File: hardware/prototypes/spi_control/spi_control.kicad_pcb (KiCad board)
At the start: 2 copper layers, 78 parts, among them J1 USB_B_Micro, J39 Versa_1, J40 Versa_2, U1 ST1L08SPU33R, U2 MCP2210-I_MQ, U3 ADAR7251, U4 BGT24_Module, Y1 12MHZ, Y2 40MHz

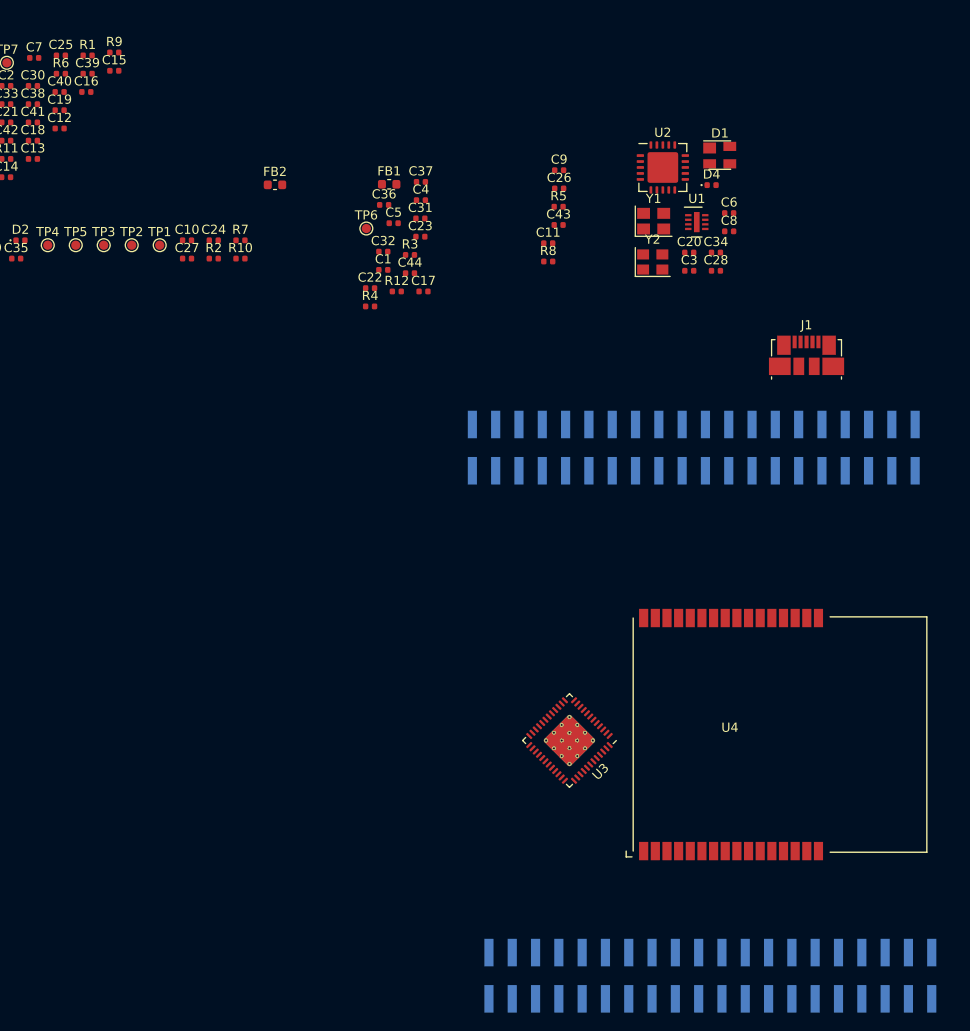
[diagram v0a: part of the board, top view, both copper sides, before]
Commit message: Fixed 3D Model path for the RF castelation board. Added mounting holes for antenna secure.
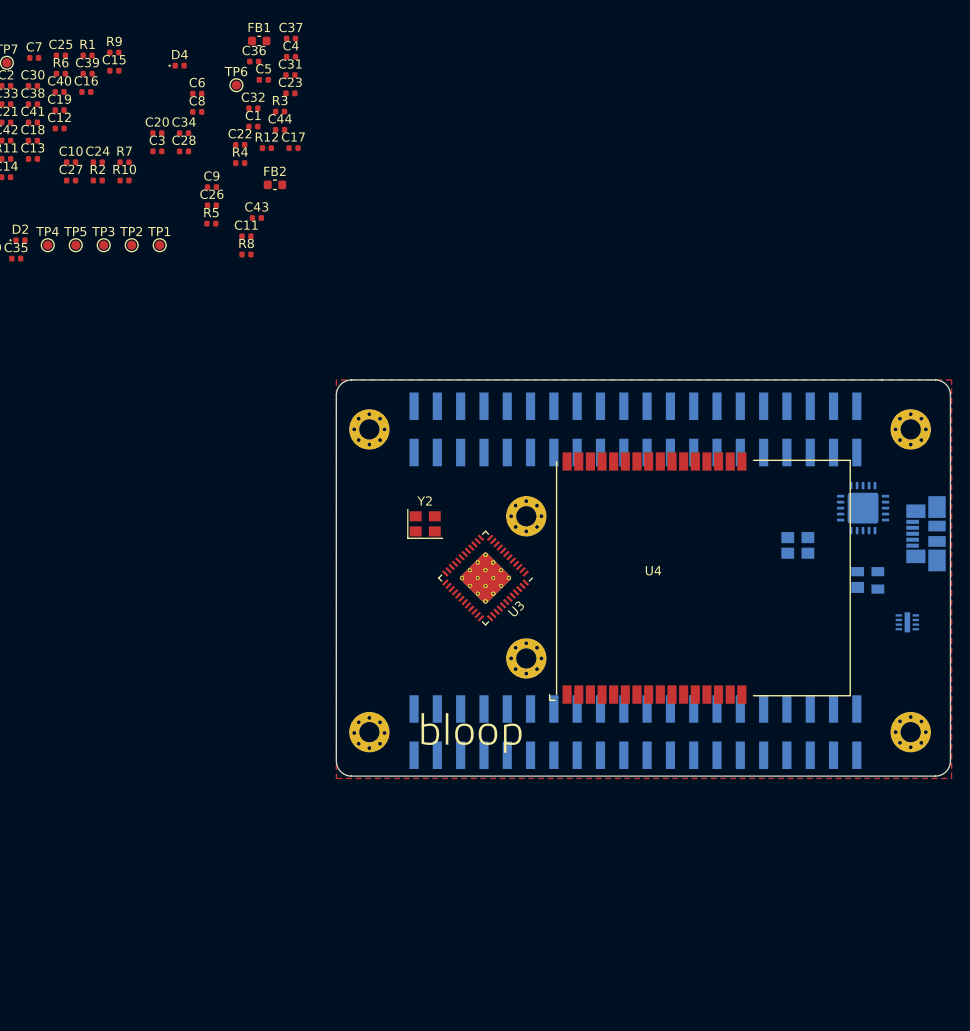
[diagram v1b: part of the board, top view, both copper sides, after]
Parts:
- added REF**: MountingHole_2.2mm_M2_Pad_Via, MountingHole:MountingHole_2.2mm_M2_Pad_Via, F.Cu at (78.1, 85.0)
- added REF**: MountingHole_2.2mm_M2_Pad_Via, MountingHole:MountingHole_2.2mm_M2_Pad_Via, F.Cu at (78.1, 69.5)
- added REF**: MountingHole_2.2mm_M2_Pad_Via, MountingHole:MountingHole_2.2mm_M2_Pad_Via, F.Cu at (120.0, 93.0)
- added REF**: MountingHole_2.2mm_M2_Pad_Via, MountingHole:MountingHole_2.2mm_M2_Pad_Via, F.Cu at (120.0, 60.0)
- added REF**: MountingHole_2.2mm_M2_Pad_Via, MountingHole:MountingHole_2.2mm_M2_Pad_Via, F.Cu at (61.0, 93.1)
- added REF**: MountingHole_2.2mm_M2_Pad_Via, MountingHole:MountingHole_2.2mm_M2_Pad_Via, F.Cu at (61.0, 60.0)
- added ~: LOGO, bloop:bloop_logo_text_silkandcopper, F.Cu at (72.1, 93.2)
- D1, J1, U1, U2, Y1: moved to B.Cu
- moved C20 59.4 mm to (37.9, 27.7)
- moved C28 59.4 mm to (40.8, 29.7)
- moved C3 59.4 mm to (37.9, 29.7)
- moved C34 59.4 mm to (40.8, 27.7)
- moved D4 59.4 mm to (40.3, 20.4)
- moved C6 59.4 mm to (42.2, 23.4)
- moved C8 59.4 mm to (42.2, 25.4)
- moved U1 49.3 mm to (119.6, 81.0)
- moved D1 49.1 mm to (115.3, 76.5)
- moved U2 43.1 mm to (114.8, 68.6)
- moved Y1 38.7 mm to (107.7, 72.6)
- moved C26 37.9 mm to (43.8, 35.6)
- moved C9 37.9 mm to (43.8, 33.6)
- moved R5 37.9 mm to (43.8, 37.6)
- moved Y2 37.8 mm to (67.1, 70.3)
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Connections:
- J39 pad 10: /SCK -> /ADC_DOUT4
- J39 pad 11: Net-(J39-Pad11) -> /MISO
- J39 pad 12: Net-(J39-Pad12) -> /ADC_DOUT3
- J39 pad 13: Net-(J39-Pad13) -> /PLL_DIV_MCU
- J39 pad 14: Net-(J39-Pad14) -> /ADC_DOUT2
- J39 pad 15: Net-(J39-Pad15) -> /PLL_LE
- J39 pad 16: /PLL_CS -> /ADC_DOUT1
- J39 pad 17: Net-(J39-Pad17) -> /PLL_CS
- J39 pad 18: /PLL_LE -> /ADC_DOUT0
- J39 pad 20: /PLL_DIV_MCU -> Net-(J39-Pad20)
- J39 pad 29: Net-(J39-Pad29) -> /~CONV_START
- J39 pad 31: Net-(J39-Pad31) -> /~FAULT
- J39 pad 33: Net-(J39-Pad33) -> /~RESET\PWDN
- J39 pad 4: Net-(J39-Pad4) -> /ADC_DOUT7
- J39 pad 5: Net-(J39-Pad5) -> /SCLK_ADC
- J39 pad 6: /MISO -> /ADC_DOUT6
- J39 pad 7: Net-(J39-Pad7) -> /SCK
- J39 pad 8: /MOSI -> /ADC_DOUT5
- J39 pad 9: Net-(J39-Pad9) -> /MOSI
- J40 pad 1: /ADC_DOUT7 -> /DATA_READY
- J40 pad 11: /ADC_DOUT2 -> Net-(J40-Pad11)
- J40 pad 13: /ADC_DOUT1 -> Net-(J40-Pad13)
- J40 pad 15: /ADC_DOUT0 -> Net-(J40-Pad15)
- J40 pad 17: /SCLK_ADC -> Net-(J40-Pad17)
- J40 pad 3: /ADC_DOUT6 -> Net-(J40-Pad3)
- J40 pad 5: /ADC_DOUT5 -> /MCLKIN
- J40 pad 7: /ADC_DOUT4 -> Net-(J40-Pad7)
- J40 pad 9: /ADC_DOUT3 -> Net-(J40-Pad9)
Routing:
- added copper zone on F.Cu, net GND
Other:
- board outline added: 66.9 x 43.2 mm

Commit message: Aligned all holes to by symmetric and locked their position
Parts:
- moved C11 38.1 mm to (46.3, 77.0)
- moved C20 38.1 mm to (36.6, 65.8)
- moved C21 38.1 mm to (20.2, 64.6)
- moved C22 38.1 mm to (45.6, 67.1)
- moved C33 38.1 mm to (20.2, 62.7)
- moved C34 38.1 mm to (39.5, 65.8)
- moved C38 38.1 mm to (23.1, 62.7)
- moved C41 38.1 mm to (23.1, 64.6)
- moved TP6 38.1 mm to (45.2, 60.6)
- moved C12 38.1 mm to (26.0, 65.3)
- moved C14 38.1 mm to (20.1, 70.6)
- moved C15 38.1 mm to (31.9, 59.0)
- moved C17 38.1 mm to (51.5, 67.4)
- moved C18 38.1 mm to (23.1, 66.6)
- moved C19 38.1 mm to (26.0, 63.3)
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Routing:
- added copper zone on B.Cu, net (none)
- added copper zone on In2.Cu, net +3V3
- added copper zone on In1.Cu, net GND
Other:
- copper layers 2 -> 4
- board text added: "Top - SIGNAL Inner Layer 1 - GND Inner Layer 2 - Power Bottom - SIGNAL"

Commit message: Found error in layer stackup, fixed net for top copper.
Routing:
- added copper zone on F.Cu, net (none)
- removed copper zone on F.Cu, net GND
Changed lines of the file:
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@@
       (xy 1.499932 -3.114028) (xy 1.609258 -3.12054) (xy 1.718859 -3.123741) (xy 1.828668 -3.123619)) (layer F.Mask) (width 0.127))
   )
-  (module MountingHole:MountingHole_2.2mm_M2_Pad_Via (layer F.Cu)
+  (module MountingHole:MountingHole_2.2mm_M2_Pad_Via locked (layer F.Cu)
     (at 77.47 84.411)
     (descr "Mounting Hole 2.2mm, M2")
@@
     (pad 1 thru_hole circle (at 0 0) (size 4.4 4.4) (drill 2.2) (layers *.Cu *.Mask))
   )
-  (module MountingHole:MountingHole_2.2mm_M2_Pad_Via (layer F.Cu)
+  (module MountingHole:MountingHole_2.2mm_M2_Pad_Via locked (layer F.Cu)
     (at 77.47 68.58)
     (descr "Mounting Hole 2.2mm, M2")
@@
     (pad 1 thru_hole circle (at 0 0) (size 4.4 4.4) (drill 2.2) (layers *.Cu *.Mask))
   )
-  (module MountingHole:MountingHole_2.2mm_M2_Pad_Via (layer F.Cu)
+  (module MountingHole:MountingHole_2.2mm_M2_Pad_Via locked (layer F.Cu)
     (at 120 92.9946)
     (descr "Mounting Hole 2.2mm, M2")
@@
     (pad 1 thru_hole circle (at 0 0) (size 4.4 4.4) (drill 2.2) (layers *.Cu *.Mask))
   )
-  (module MountingHole:MountingHole_2.2mm_M2_Pad_Via (layer F.Cu)
+  (module MountingHole:MountingHole_2.2mm_M2_Pad_Via locked (layer F.Cu)
     (at 120 60)
     (descr "Mounting Hole 2.2mm, M2")
@@
     (pad 1 thru_hole circle (at 0 0) (size 4.4 4.4) (drill 2.2) (layers *.Cu *.Mask))
   )
-  (module MountingHole:MountingHole_2.2mm_M2_Pad_Via (layer F.Cu)
+  (module MountingHole:MountingHole_2.2mm_M2_Pad_Via locked (layer F.Cu)
     (at 61 93.091)
     (descr "Mounting Hole 2.2mm, M2")
@@
     (pad 1 thru_hole circle (at 0 -0.0964) (size 4.4 4.4) (drill 2.2) (layers *.Cu *.Mask))
   )
-  (module MountingHole:MountingHole_2.2mm_M2_Pad_Via (layer F.Cu)
+  (module MountingHole:MountingHole_2.2mm_M2_Pad_Via locked (layer F.Cu)
     (at 61 60)
     (descr "Mounting Hole 2.2mm, M2")
@@
     )
   )
-  (zone (net 1) (net_name GND) (layer F.Cu) (hatch edge 0.508)
+  (zone (net 0) (net_name "") (layer F.Cu) (hatch edge 0.508)
     (connect_pads yes (clearance 0.3))
     (min_thickness 0.254)

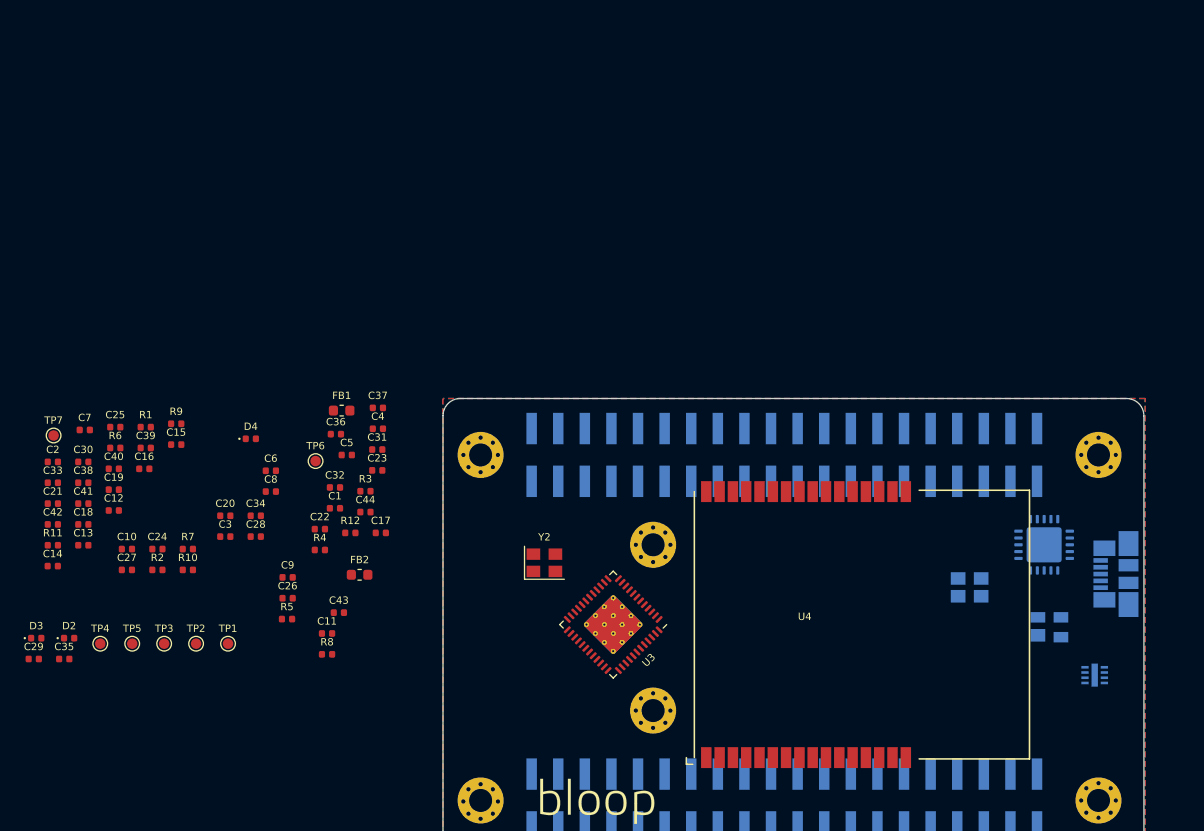
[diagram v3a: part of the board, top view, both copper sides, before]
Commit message: finished routing power section
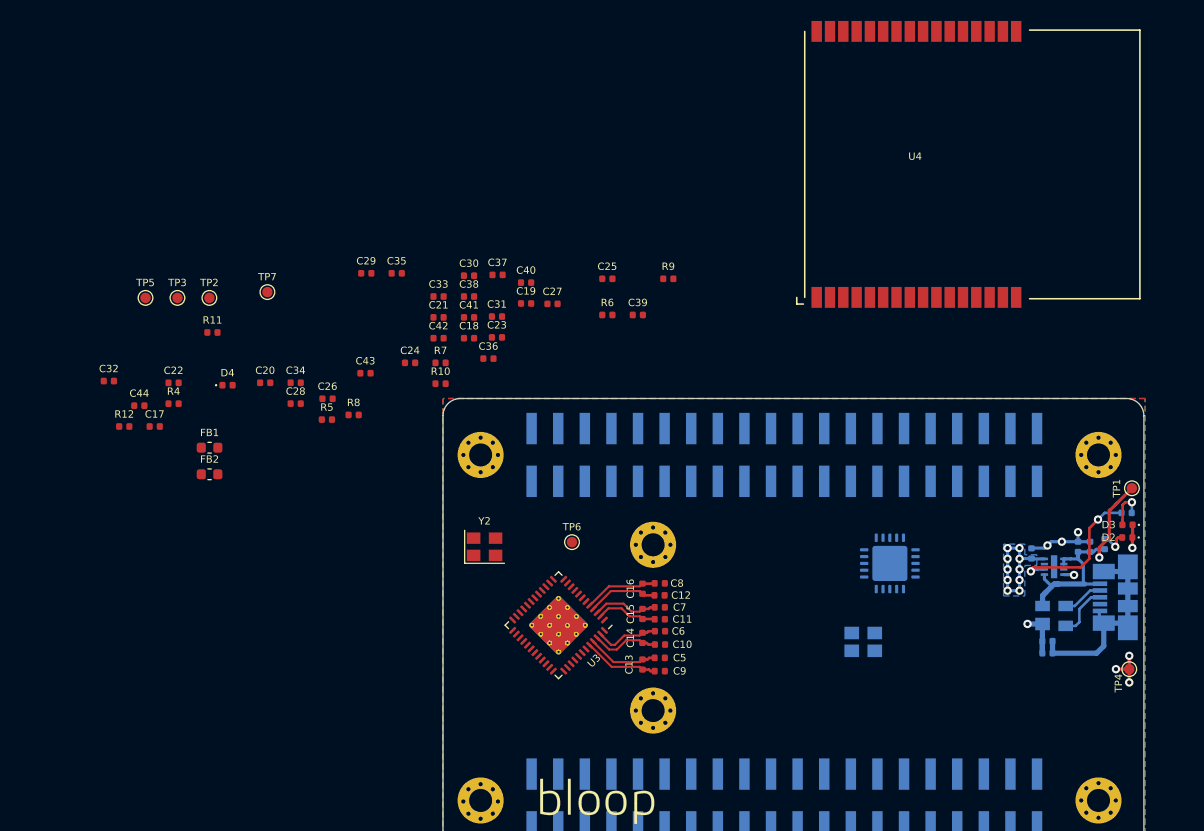
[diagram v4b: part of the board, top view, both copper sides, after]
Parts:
- C1, C2, C3, C4, R1, R2, R3: moved to B.Cu
- moved D3 104.8 mm to (122.8, 66.7), turned to 180 degrees
- moved D2 101.5 mm to (122.7, 67.9), turned to 180 degrees
- moved TP4 98.3 mm to (122.9, 80.5), turned to 90 degrees
- moved C2 98.2 mm to (118.0, 68.8), turned to 90 degrees
- moved R2 90.5 mm to (120.6, 68.5), turned to 270 degrees
- moved R1 88.8 mm to (115.1, 78.9), turned to 180 degrees
- moved TP1 87.6 mm to (123.2, 63.2), turned to 90 degrees
- moved C3 82.6 mm to (119.2, 68.8), turned to 90 degrees
- moved R3 72.7 mm to (122.7, 65.5), turned to 180 degrees
- moved C1 69.2 mm to (115.1, 77.8), turned to 180 degrees
- moved C4 63.5 mm to (113.6, 69.4), turned to 90 degrees
- moved C7 57.5 mm to (78.1, 74.5), turned to 180 degrees
- moved C14 56.7 mm to (76.5, 77.5), turned to 270 degrees
- moved C13 54.6 mm to (76.5, 80.0), turned to 270 degrees
- moved C12 52.7 mm to (78.1, 73.4), turned to 180 degrees
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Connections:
- D1 pad 3: /USB_D+ -> /USB_D-
- D1 pad 4: /USB_D- -> /USB_D+
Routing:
- net /5V_USB: track 0.00 -> 26.5 mm, vias 0 -> 1
- net GNDREF: track 0.00 -> 20.6 mm
- net GND: track 0.00 -> 19.9 mm, vias 0 -> 9
- net Net-(R3-Pad2): track 0.00 -> 14.2 mm, vias 0 -> 2
- net +3V3: track 0.00 -> 13.7 mm, vias 0 -> 10
- net /F_IF1_Q+: track 0.00 -> 7.24 mm
- net /F_IF2_I-: track 0.00 -> 7.08 mm
- net /F_IF1_Q-: track 0.00 -> 6.86 mm
- net /F_IF2_I+: track 0.00 -> 6.73 mm
- net /F_IF1_I+: track 0.00 -> 6.53 mm
- net /F_IF2_Q-: track 0.00 -> 6.35 mm
- net /F_IF1_I-: track 0.00 -> 6.16 mm
- net /F_IF2_Q+: track 0.00 -> 5.92 mm
- net /USB_D+: track 0.00 -> 5.14 mm
- net Net-(D3-Pad2): track 0.00 -> 3.93 mm, vias 0 -> 1
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- added copper zone on B.Cu, net +3V3
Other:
- net class Power added: clearance 0.2, trace_width 0.3, via_dia 0.8, via_drill 0.4

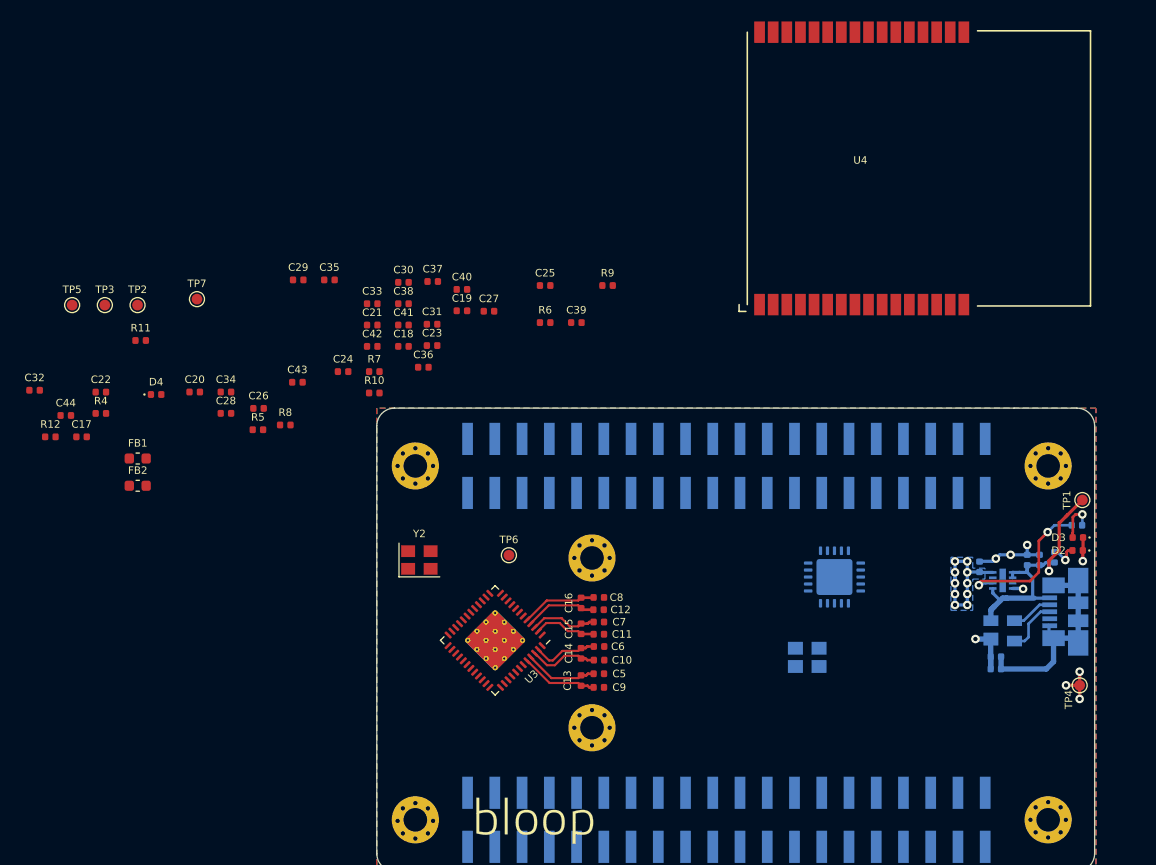
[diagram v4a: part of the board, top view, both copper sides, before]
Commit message: Started routing SPI to USB. Started preliminary routing for the IQ data.
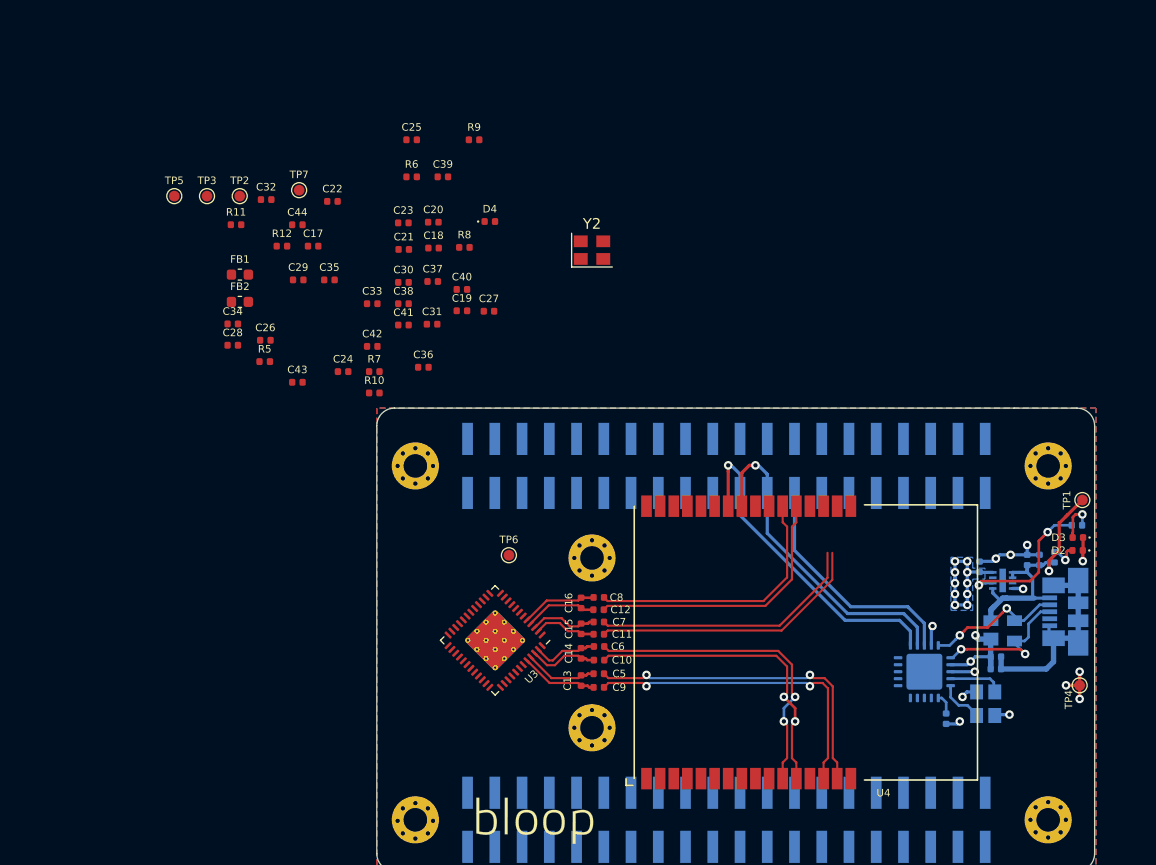
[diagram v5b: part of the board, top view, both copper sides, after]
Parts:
- R4: moved to B.Cu
- moved R4 83.8 mm to (110.5, 83.6), turned to 270 degrees
- moved U4 45.4 mm to (101.6, 89.2)
- moved D4 35.0 mm to (67.9, 37.2)
- moved Y2 33.1 mm to (77.5, 39.9)
- moved C32 28.0 mm to (47.1, 35.2)
- moved R12 28.0 mm to (48.6, 39.5)
- moved C17 28.0 mm to (51.5, 39.5)
- moved C22 28.0 mm to (53.3, 35.3)
- moved C44 28.0 mm to (50.0, 37.5)
- moved C20 27.3 mm to (62.7, 37.3)
- moved R8 23.5 mm to (65.6, 39.6)
- moved FB1 19.6 mm to (44.6, 42.2)
- moved FB2 19.6 mm to (44.6, 44.7)
- moved C25 18.4 mm to (60.7, 29.6)
- moved C39 18.4 mm to (63.6, 33.0)
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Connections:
- J40 pad 21: /PLL_RSET -> /PLL_MOD
- J40 pad 25: /PLL_MOD -> /PLL_RSET
- Y1 pad 2: Net-(C23-Pad2) -> GND
- Y1 pad 3: (no net) -> Net-(C23-Pad2)
- Y1 pad 4: (no net) -> GND
- Y2 pad 2: Net-(C25-Pad2) -> GND
- Y2 pad 3: (no net) -> Net-(C25-Pad2)
- Y2 pad 4: (no net) -> GND
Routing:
- net /PLL_MUX: track 0.00 -> 31.3 mm, vias 0 -> 1
- net /PLL_MOD: track 0.00 -> 31.2 mm, vias 0 -> 1
- net /IF1_Q-: track 0.00 -> 31.1 mm, vias 0 -> 2
- net /IF1_Q+: track 0.00 -> 30.3 mm, vias 0 -> 2
- net /IF1_I-: track 0.00 -> 29.7 mm, vias 0 -> 2
- net /IF1_I+: track 0.00 -> 28.9 mm, vias 0 -> 2
- net /IF2_Q+: track 0.00 -> 25.9 mm
- net /IF2_I+: track 0.00 -> 25.7 mm
- net /IF2_Q-: track 0.00 -> 25.2 mm
- net /IF2_I-: track 0.00 -> 24.9 mm
- net /PLL_RSET: track 0.00 -> 22.3 mm
- net /USB_D-: track 3.89 -> 13.2 mm, vias 0 -> 2
- net /USB_D+: track 5.14 -> 14.2 mm, vias 0 -> 2
- net GND: track 19.9 -> 27.3 mm, vias 9 -> 12
- net Net-(C21-Pad2): track 0.00 -> 5.70 mm
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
